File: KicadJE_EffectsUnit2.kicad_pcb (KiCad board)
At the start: 2 copper layers, 100 x 100 mm, 70 parts, among them J201 In_1, J202 In 2, J203 Out 1, J204 Out 2, J205 Out Final, P201 Doepfer_Power_10pin, SW201 Out 1, SW202 In or cascade, SW203 Out 2 FB, SW204 In or cascade, SW205 HI/LO, U201 TL072, U202 TL072

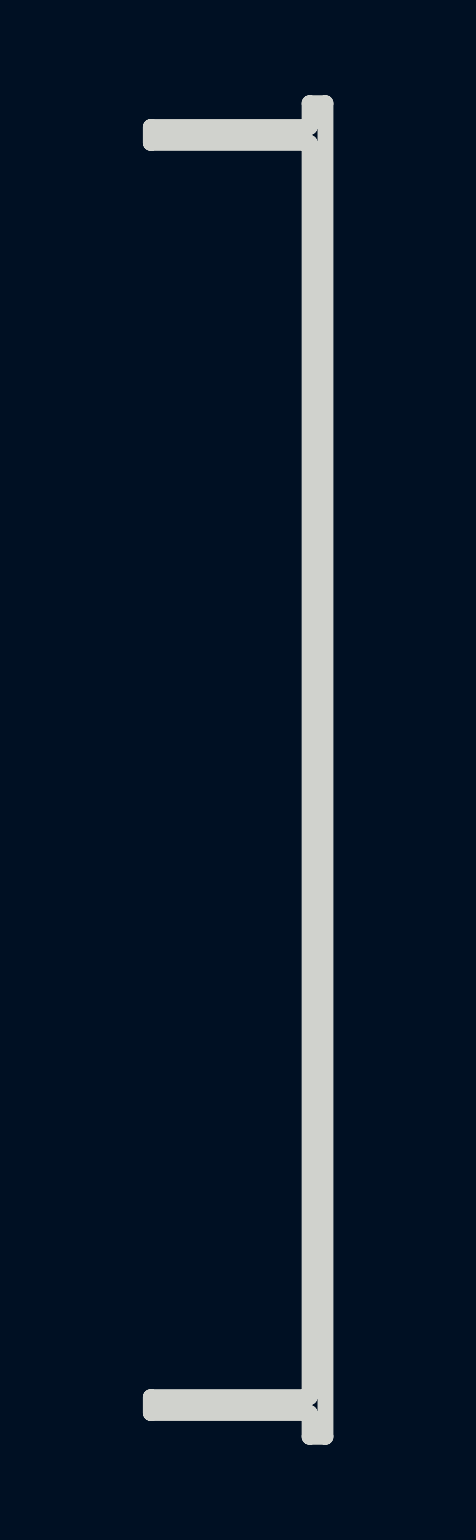
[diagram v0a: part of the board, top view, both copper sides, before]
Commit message: New base schematic for angled board
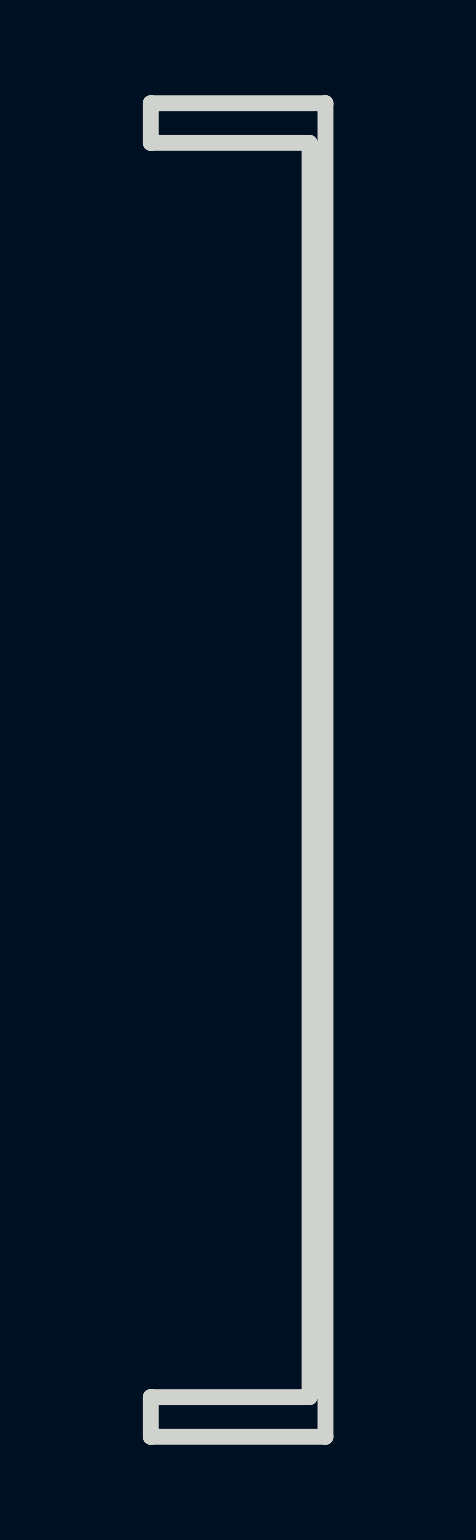
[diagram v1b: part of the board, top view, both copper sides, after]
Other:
- outline, holes or cut-outs redrawn
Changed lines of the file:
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@@
   (general
     (thickness 1.6)
-    (drawings 39)
+    (drawings 35)
     (tracks 586)
     (zones 0)
@@
     (pad 1 thru_hole circle (at 1.166726 1.166726) (size 0.7 0.7) (drill 0.4) (layers *.Cu *.Mask))
   )
-  (gr_line (start 111 58.5) (end 110 58.5) (layer Edge.Cuts) (width 1))
-  (gr_line (start 110 60) (end 110 58.5) (layer Edge.Cuts) (width 1))
-  (gr_line (start 111 142.5) (end 110 142.5) (layer Edge.Cuts) (width 1))
-  (gr_line (start 110 142.5) (end 110 141) (layer Edge.Cuts) (width 1))
-  (gr_line (start 100 61) (end 100 60) (layer Edge.Cuts) (width 1))
+  (gr_line (start 100 61) (end 100 58.5) (layer Edge.Cuts) (width 1))
   (gr_line (start 100 61) (end 110 61) (layer Edge.Cuts) (width 1))
-  (gr_line (start 110 60) (end 100 60) (layer Edge.Cuts) (width 1))
-  (gr_line (start 100 141) (end 100 140) (layer Edge.Cuts) (width 1))
-  (gr_line (start 100 141) (end 110 141) (layer Edge.Cuts) (width 1))
+  (gr_line (start 111 58.5) (end 100 58.5) (layer Edge.Cuts) (width 1))
+  (gr_line (start 100 142.5) (end 100 140) (layer Edge.Cuts) (width 1))
+  (gr_line (start 100 142.5) (end 111 142.5) (layer Edge.Cuts) (width 1))
   (gr_line (start 110 140) (end 100 140) (layer Edge.Cuts) (width 1))
   (gr_line (start 129.5 60) (end 129.5 140) (layer Edge.Cuts) (width 1))

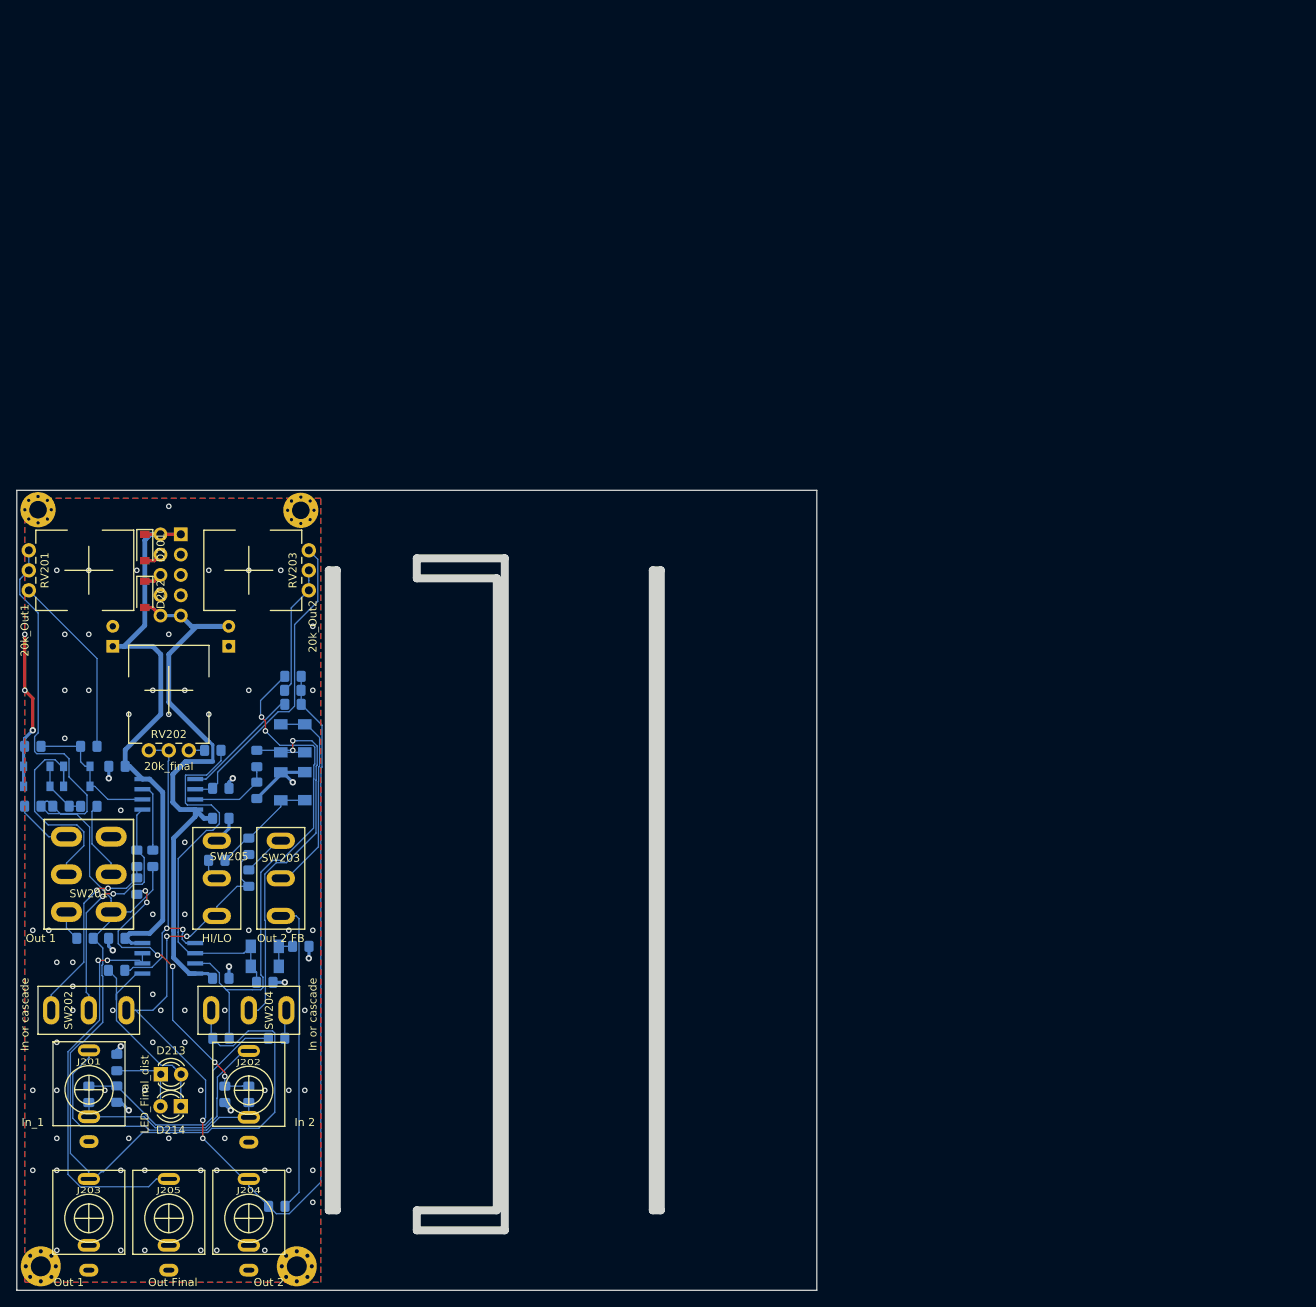
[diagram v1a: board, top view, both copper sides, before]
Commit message: Zener added to EU-7
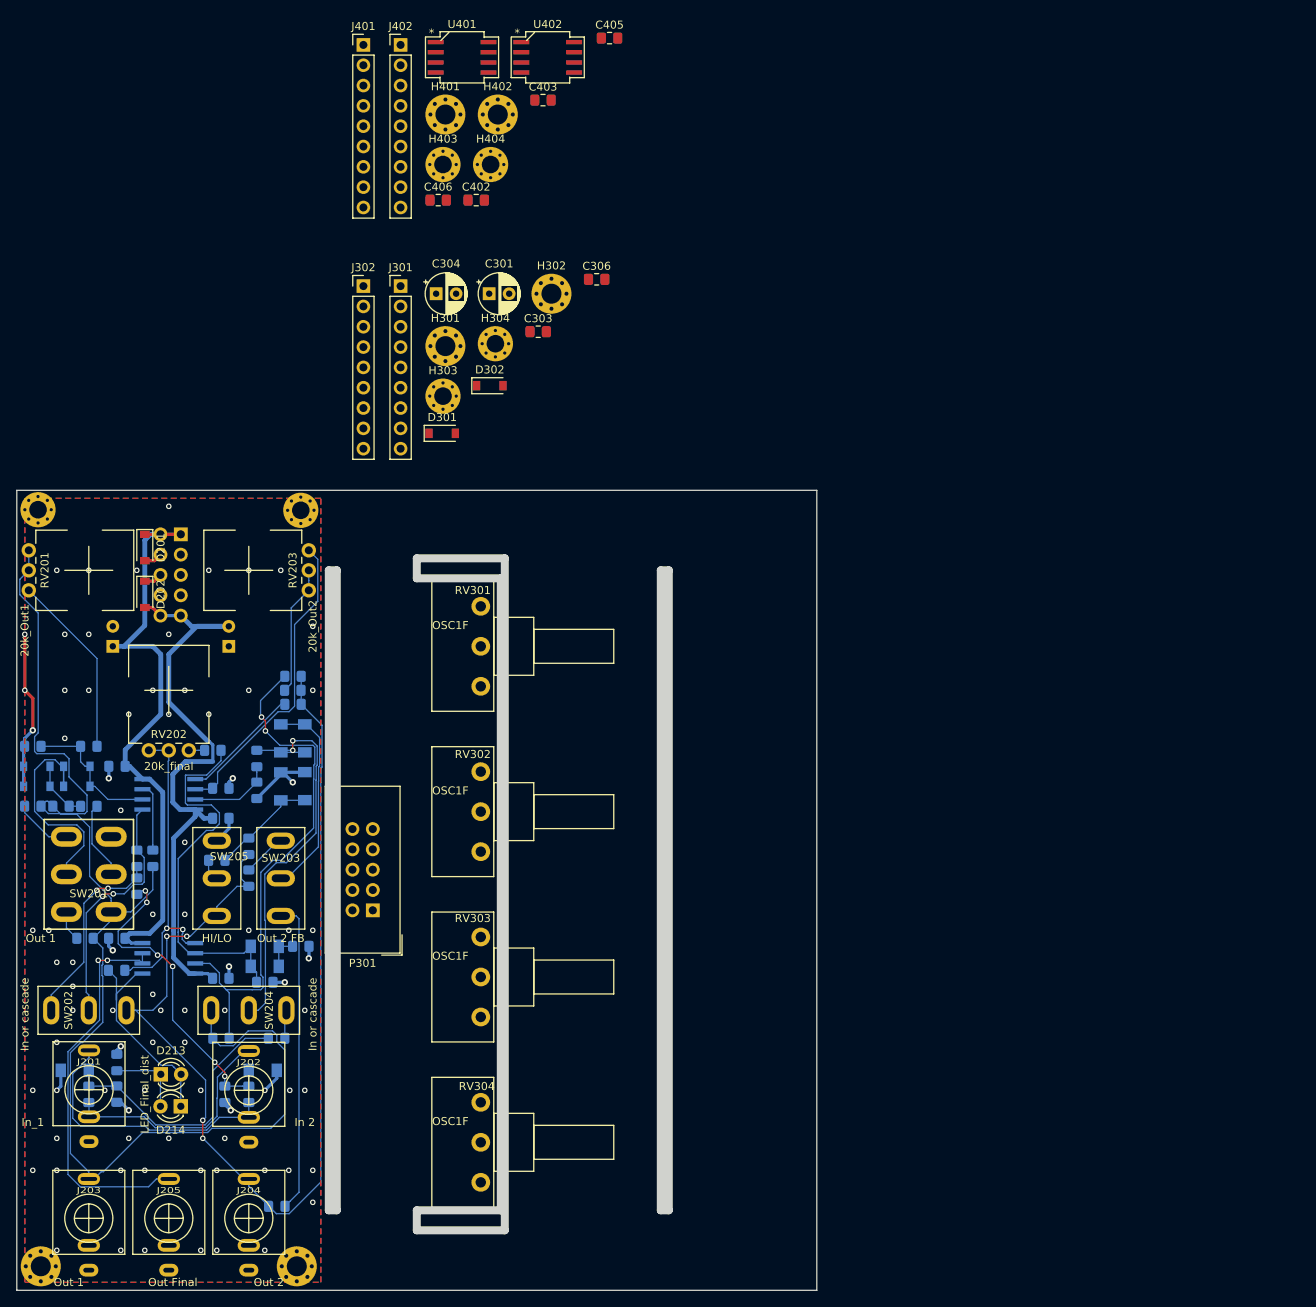
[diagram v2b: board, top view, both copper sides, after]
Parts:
- added C301: 100uF 16v, Capacitor_THT:CP_Radial_D5.0mm_P2.50mm, F.Cu at (109.0, 25.4)
- added C303: 100n, Capacitor_SMD:C_0805_2012Metric_Pad1.15x1.40mm_HandSolder, F.Cu at (115.2, 30.2)
- added C304: 100uF 16v, Capacitor_THT:CP_Radial_D5.0mm_P2.50mm, F.Cu at (102.4, 25.4)
- added C306: 100n, Capacitor_SMD:C_0805_2012Metric_Pad1.15x1.40mm_HandSolder, F.Cu at (122.5, 23.6)
- added C402: 100n, Capacitor_SMD:C_0805_2012Metric_Pad1.15x1.40mm_HandSolder, F.Cu at (107.4, 13.7)
- added C403: 100n, Capacitor_SMD:C_0805_2012Metric_Pad1.15x1.40mm_HandSolder, F.Cu at (115.8, 1.23)
- added C405: 100n, Capacitor_SMD:C_0805_2012Metric_Pad1.15x1.40mm_HandSolder, F.Cu at (124.1, -6.52)
- added C406: 100n, Capacitor_SMD:C_0805_2012Metric_Pad1.15x1.40mm_HandSolder, F.Cu at (102.7, 13.7)
- added D215: D_Zener, Diode_SMD:D_MiniMELF, B.Cu at (80.8, 122.5)
- added D216: D_Zener, Diode_SMD:D_MiniMELF, B.Cu at (57.2, 122.5)
- added D301: 1N1007, Diode_SMD:D_SOD-123, F.Cu at (103.2, 42.9)
- added D302: 1N1007, Diode_SMD:D_SOD-123, F.Cu at (109.1, 36.9)
- added H301: 2,5mm, MountingHole:MountingHole_2.5mm_Pad_Via, F.Cu at (103.6, 32.0)
- added H302: 2,5mm, MountingHole:MountingHole_2.5mm_Pad_Via, F.Cu at (116.8, 25.4)
- added H303: 2,2mm, MountingHole:MountingHole_2.2mm_M2_Pad_Via, F.Cu at (103.3, 38.2)
- added H304: 2,2mm, MountingHole:MountingHole_2.2mm_M2_Pad_Via, F.Cu at (109.8, 31.7)
- added H401: 2,5mm, MountingHole:MountingHole_2.5mm_Pad_Via, F.Cu at (103.6, 3.03)
- added H402: 2,5mm, MountingHole:MountingHole_2.5mm_Pad_Via, F.Cu at (110.1, 3.03)
- added H403: 2,2mm, MountingHole:MountingHole_2.2mm_M2_Pad_Via, F.Cu at (103.3, 9.28)
- added H404: 2,2mm, MountingHole:MountingHole_2.2mm_M2_Pad_Via, F.Cu at (109.2, 9.28)
- added J301: Conn_01x09_Male, Connector_PinHeader_2.54mm:PinHeader_1x09_P2.54mm_Vertical, F.Cu at (98.0, 24.5)
- added J302: Conn_01x09_Male, Connector_PinHeader_2.54mm:PinHeader_1x09_P2.54mm_Vertical, F.Cu at (93.3, 24.5)
- added J401: Conn_01x09_Male, Connector_PinHeader_2.54mm:PinHeader_1x09_P2.54mm_Vertical, F.Cu at (93.3, -5.67)
- added J402: Conn_01x09_Male, Connector_PinHeader_2.54mm:PinHeader_1x09_P2.54mm_Vertical, F.Cu at (98.0, -5.67)
- added P301: Doepfer_Power_10pin, Connectors_IDC:IDC-Header_2x05_Pitch2.54mm_Straight, F.Cu at (94.5, 102.5)
- added RV301: POT, Potentiometer_THT:Potentiometer_Piher_T-16H_Single_Horizontal, F.Cu at (108.0, 74.5)
- added RV302: POT, Potentiometer_THT:Potentiometer_Piher_T-16H_Single_Horizontal, F.Cu at (108.0, 95.2)
- added RV303: POT, Potentiometer_THT:Potentiometer_Piher_T-16H_Single_Horizontal, F.Cu at (108.0, 115.8)
- added RV304: POT, Potentiometer_THT:Potentiometer_Piher_T-16H_Single_Horizontal, F.Cu at (108.0, 136.5)
- added U401: TL072, AJ-Dropbox-Kicad:AJ_SO-8_5.3x6.2mm_P1.27mm, F.Cu at (105.7, -4.12)
- added U402: TL072, AJ-Dropbox-Kicad:AJ_SO-8_5.3x6.2mm_P1.27mm, F.Cu at (116.4, -4.12)
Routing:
- net GND: track 51.0 -> 56.8 mm
- net Net-(C208-Pad1): track 32.4 -> 34.3 mm
- net Net-(C204-Pad1): track 38.1 -> 40.0 mm
- net Out1Dist: track 160.7 -> 162.6 mm
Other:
- outline, holes or cut-outs redrawn

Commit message: Panel board routed
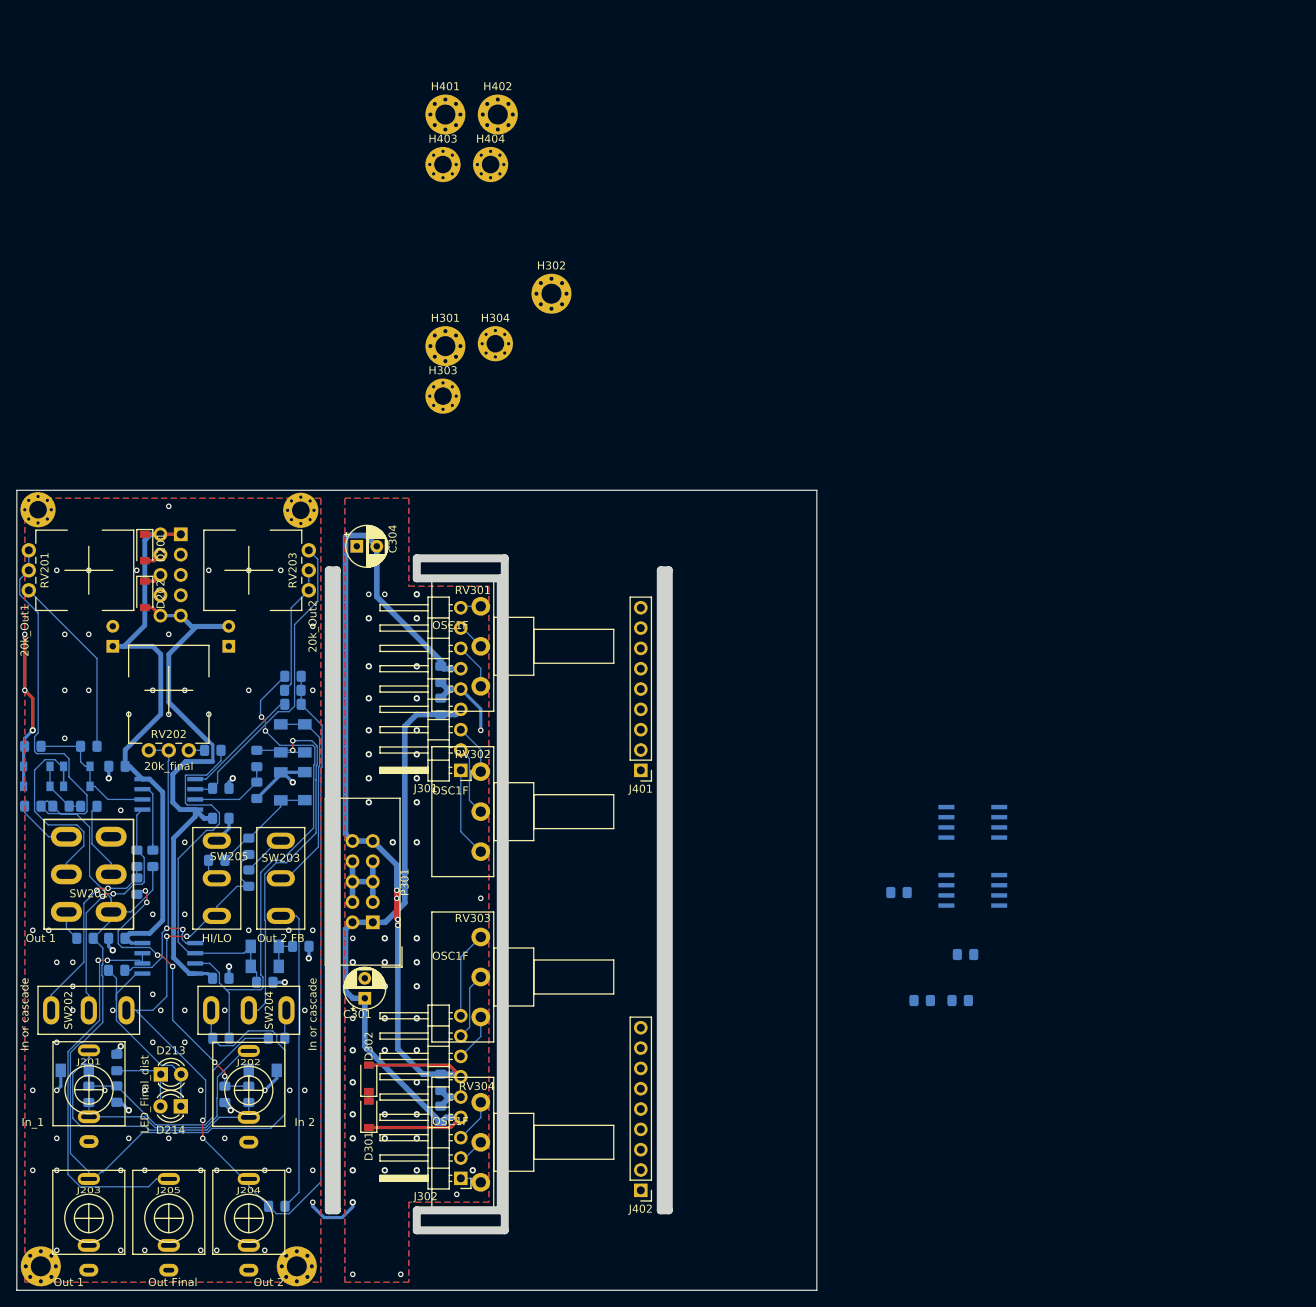
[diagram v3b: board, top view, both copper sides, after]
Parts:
- added C302: 100n, Capacitor_SMD:C_0805_2012Metric_Pad1.15x1.40mm_HandSolder, B.Cu at (103.0, 128.0)
- added C305: 100n, Capacitor_SMD:C_0805_2012Metric_Pad1.15x1.40mm_HandSolder, B.Cu at (103.0, 124.0)
- C303, C306, C402, C403, C405, C406, U401, U402: moved to B.Cu
- J301, J302: footprint Connector_PinHeader_2.54mm:PinHeader_1x09_P2.54mm_Vertical -> Connector_PinHeader_2.54mm:PinHeader_1x09_P2.54mm_Horizontal
- moved J402 146.3 mm to (128.0, 137.5), turned to 180 degrees
- moved C405 122.9 mm to (168.6, 108.0)
- moved U401 122.1 mm to (169.5, 100.0)
- moved C402 116.9 mm to (167.9, 113.8)
- moved C406 116.9 mm to (163.2, 113.8)
- moved J302 112.2 mm to (105.5, 136.0), turned to 180 degrees
- moved U402 109.4 mm to (169.5, 91.5)
- moved C403 108.6 mm to (160.3, 100.3)
- moved J401 97.1 mm to (128.0, 85.0), turned to 180 degrees
- moved C301 89.4 mm to (93.5, 113.5), turned to 90 degrees
- moved D302 87.9 mm to (94.0, 123.5), turned to 90 degrees
- moved D301 85.6 mm to (94.0, 128.0), turned to 90 degrees
- moved J301 61.0 mm to (105.5, 85.0), turned to 180 degrees
- moved C306 53.1 mm to (103.0, 73.0), turned to 270 degrees
- moved C303 48.4 mm to (103.0, 77.0), turned to 270 degrees
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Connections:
- C301 pad 1: /angled_panel/-12v -> -12V
- C303 pad 2: /angled_panel/-12v -> -12V
- C304 pad 2: /angled_panel/+12v -> +12V
- C306 pad 1: /angled_panel/+12v -> +12V
- D301 pad 1: /angled_panel/-12v -> -12V
- D302 pad 2: /angled_panel/+12v -> +12V
- J301 pad 6: -12V -> +12V
- J302 pad 4: +12V -> -12V
- P301 pad 1: /angled_panel/-12v -> -12V
- P301 pad 10: /angled_panel/+12v -> +12V
- P301 pad 2: /angled_panel/-12v -> -12V
- P301 pad 9: /angled_panel/+12v -> +12V
- RV301 pad 1: /KicadJE_EU8_Dist/POT1_H -> /KicadJE_EU8_Dist/POT1_L
- RV301 pad 3: /KicadJE_EU8_Dist/POT1_L -> /KicadJE_EU8_Dist/POT1_H
- RV302 pad 1: /KicadJE_EU8_Dist/POT2_H -> /KicadJE_EU8_Dist/POT2_L
- RV302 pad 3: /KicadJE_EU8_Dist/POT2_L -> /KicadJE_EU8_Dist/POT2_H
- RV303 pad 1: /KicadJE_EU8_Dist/POT3_H -> /KicadJE_EU8_Dist/POT3_L
- RV303 pad 3: /KicadJE_EU8_Dist/POT3_L -> /KicadJE_EU8_Dist/POT3_H
- RV304 pad 1: /KicadJE_EU8_Dist/POT4_H -> /KicadJE_EU8_Dist/POT4_L
- RV304 pad 3: /KicadJE_EU8_Dist/POT4_L -> /KicadJE_EU8_Dist/POT4_H
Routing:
- net +12V: track 0.00 -> 116.8 mm, vias 0 -> 4
- net -12V: track 0.00 -> 83.5 mm
- net GND: track 56.8 -> 94.2 mm, vias 83 -> 133
- net /KicadJE_EU8_Dist/POT2_L: track 0.00 -> 11.2 mm
- net /KicadJE_EU8_Dist/POT3_H: track 0.00 -> 10.9 mm
- net /KicadJE_EU8_Dist/POT2_C: track 0.00 -> 8.74 mm
- net /KicadJE_EU8_Dist/POT3_C: track 0.00 -> 8.42 mm
- net /KicadJE_EU8_Dist/POT2_H: track 0.00 -> 6.28 mm
- net /KicadJE_EU8_Dist/POT3_L: track 0.00 -> 5.96 mm
- net /KicadJE_EU8_Dist/POT1_L: track 0.00 -> 5.78 mm
- net /KicadJE_EU8_Dist/POT4_H: track 0.00 -> 5.46 mm
- net /KicadJE_EU8_Dist/POT1_C: track 0.00 -> 3.44 mm
- net /KicadJE_EU8_Dist/POT4_C: track 0.00 -> 3.31 mm
- net /KicadJE_EU8_Dist/POT4_L: track 0.00 -> 2.71 mm
- net /KicadJE_EU8_Dist/POT1_H: track 0.00 -> 2.57 mm
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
